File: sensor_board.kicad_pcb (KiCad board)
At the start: 4 copper layers, 50 x 34 mm, 66 parts, among them J1 CORTEX-SWD-6, J2 Conn_01x04_MountingPin, J3 Conn_01x10_MountingPin, Q1 SI2337DS-T1-BE3, Q2 SI2337DS-T1-BE3, Q3 BSH203,215, U1 ATSAMC21E17A, U2 TCAN332G, U3 NCP718xSN330, U4 LMZM23600V5, U5 SHT30-DIS, U6 BMP384, U7 SCD4x, U8 SGP30, U9 BH1751FVI, Y1 Resonator

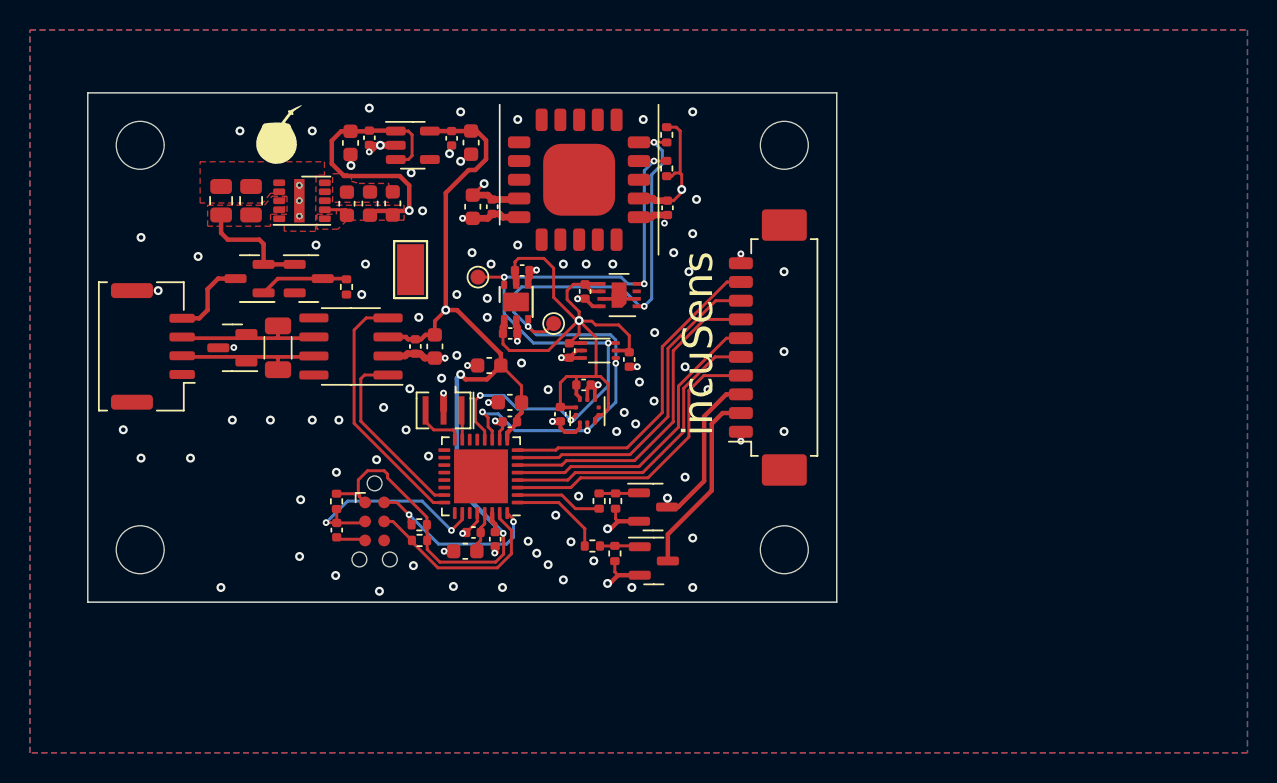
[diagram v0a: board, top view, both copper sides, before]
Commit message: added new ldo and some text
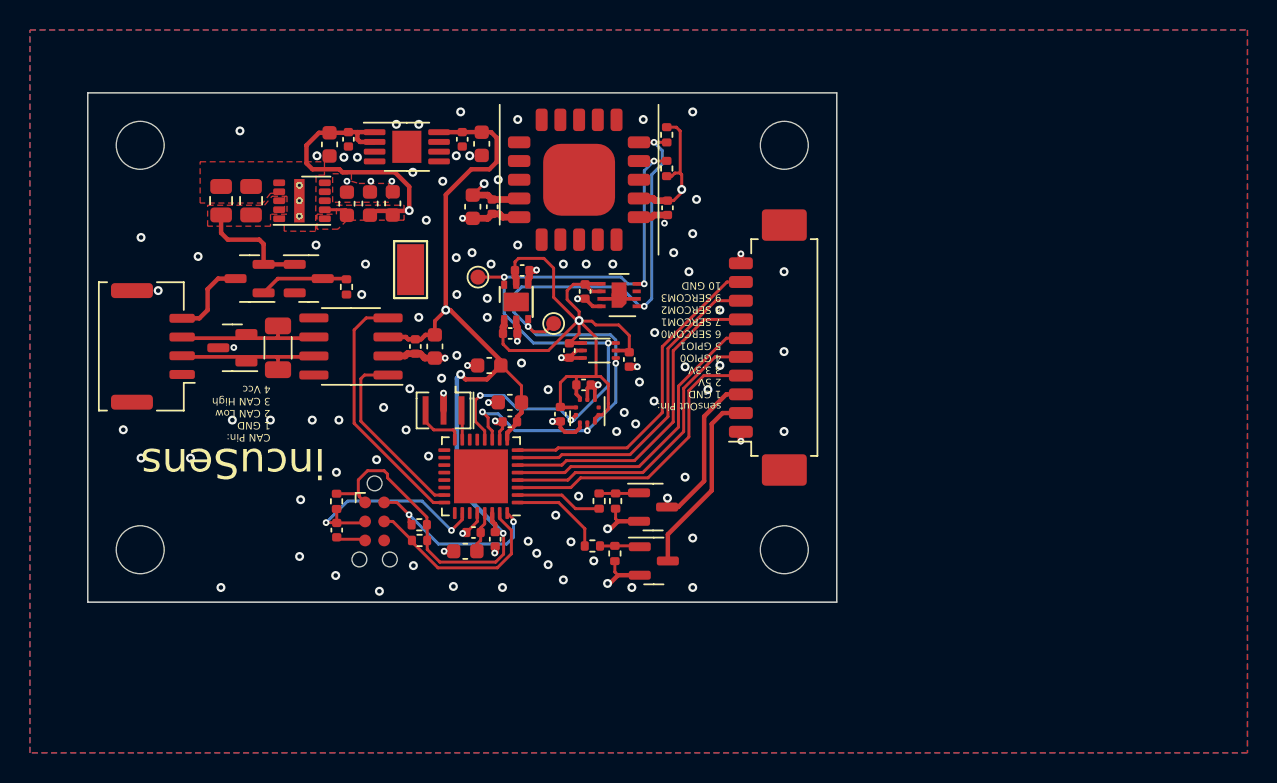
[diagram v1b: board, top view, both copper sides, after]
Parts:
- removed the G*** at (12.6, 2.80)
- added G***: LOGO, ownLib:LogoMate7x7, B.Cu at (29.6, 27.4)
- U3: value NCP718xSN330 -> TPS7B82-Q1; footprint Package_TO_SOT_SMD:SOT-23-5 -> Package_SO:MSOP-8-1EP_3x3mm_P0.65mm_EP1.95x2.15mm
- moved C13 1.40 mm to (17.4, 3.10)
- moved C12 1.40 mm to (16.1, 3.44)
- moved C15 0.71 mm to (26.3, 3.40)
- moved C14 0.71 mm to (25.0, 3.10)
- moved U3 0.41 mm to (21.3, 3.60)
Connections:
- U3 pad 2: GND -> +5V
- U3 pad 3: +5V -> GND
- U3 pad 4: unconnected-(U3-Pad4) -> GND
- U3 pad 5: VDD -> GND
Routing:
- net GND: track 37.9 -> 36.0 mm, vias 102 -> 110
- net VDD: track 94.5 -> 95.1 mm

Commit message: changed ldo cap value
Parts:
- C12: value 1uF / 10V -> 22 uF / 10V
- C15: value 1uF / 6.3V -> 22 uF / 6.3V
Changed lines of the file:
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@@
       (effects (font (size 1 1) (thickness 0.15)))
     )
-    (fp_text value "1uF / 6.3V" (at 0 1.43 90) (layer "F.Fab") hide
+    (fp_text value "22 uF / 6.3V" (at 0 1.43 90) (layer "F.Fab") hide
       (effects (font (size 1 1) (thickness 0.15)))
     )
@@
       (effects (font (size 1 1) (thickness 0.15)))
     )
-    (fp_text value "1uF / 10V" (at 0 1.43 90) (layer "F.Fab") hide
-      (effects (font (size 1 1) (thickness 0.15)))
-    )
+    (fp_text value "22 uF / 10V" (at 0 1.43 90) (layer "F.Fab") hide
+      (effects (font (size 1 1) (thickness 0.15)))
+    )

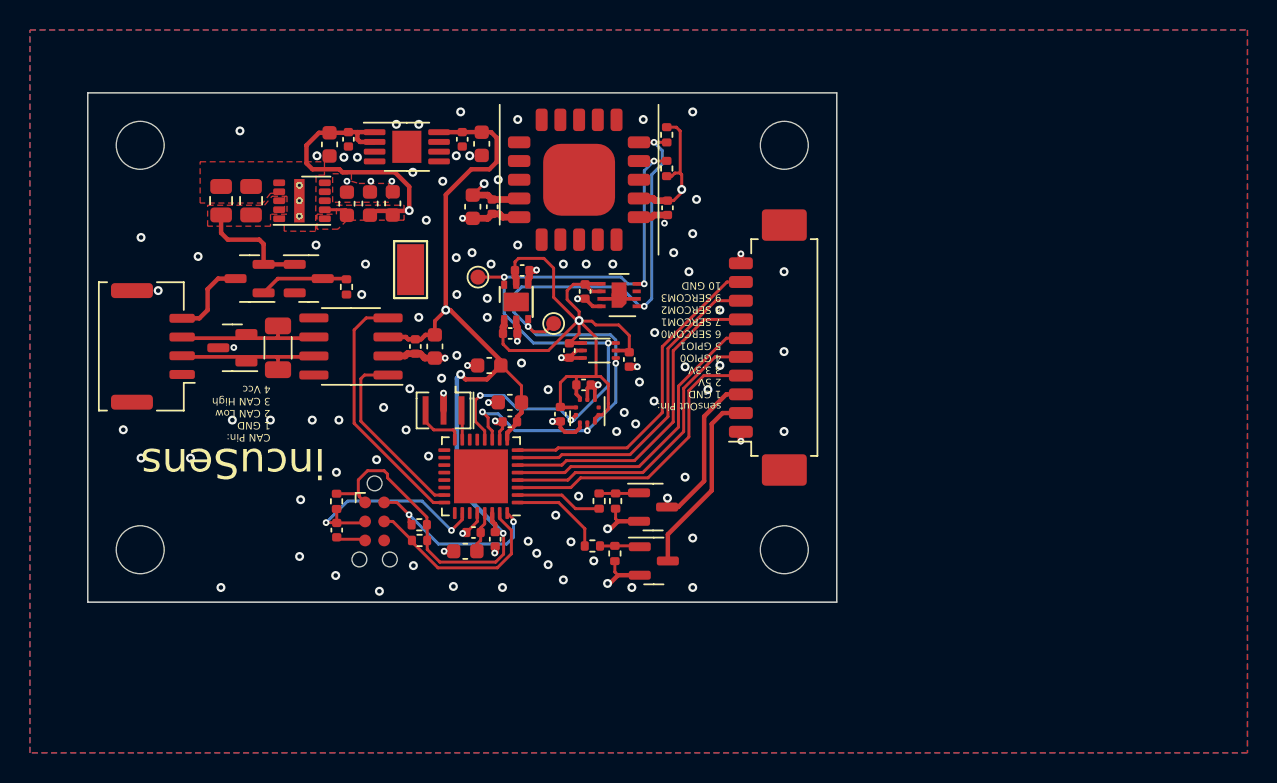
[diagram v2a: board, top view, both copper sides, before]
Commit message: changed wrong footprint of light sensor and added gitignore
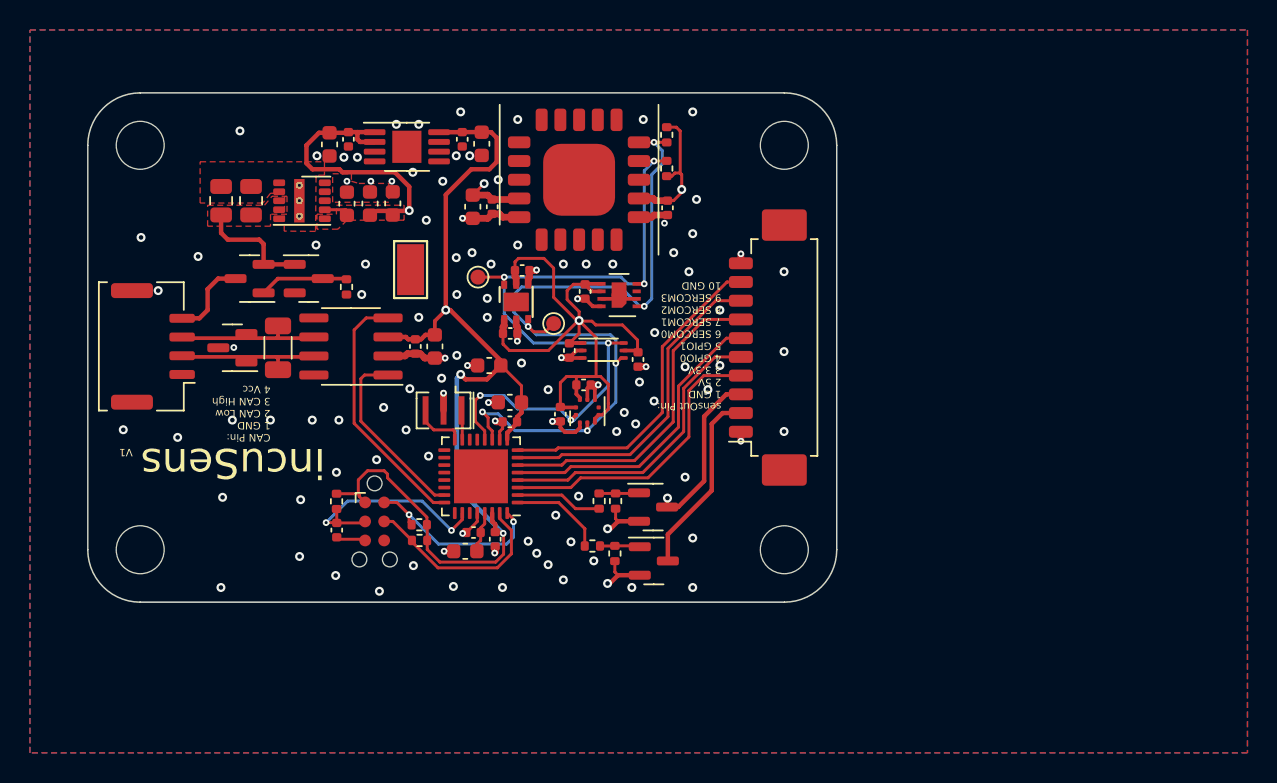
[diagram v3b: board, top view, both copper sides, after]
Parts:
- moved U9 1.44 mm to (34.4, 17.2), turned to 0 degrees
- moved C28 0.58 mm to (36.7, 17.8)
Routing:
- net /I2C.SCL: track 50.2 -> 50.7 mm
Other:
- outline, holes or cut-outs redrawn
- board text added: "V1"
